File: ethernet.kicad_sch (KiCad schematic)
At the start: 116 parts, among them IC2 ACPL-217-500E, J2 5-2337992-8, U13 TPS2372-3RGWR, U16 TS3L500, U6 KSZ9031RNXCA, Y1 ABM8G-25.000MHZ-18-D2Y-T

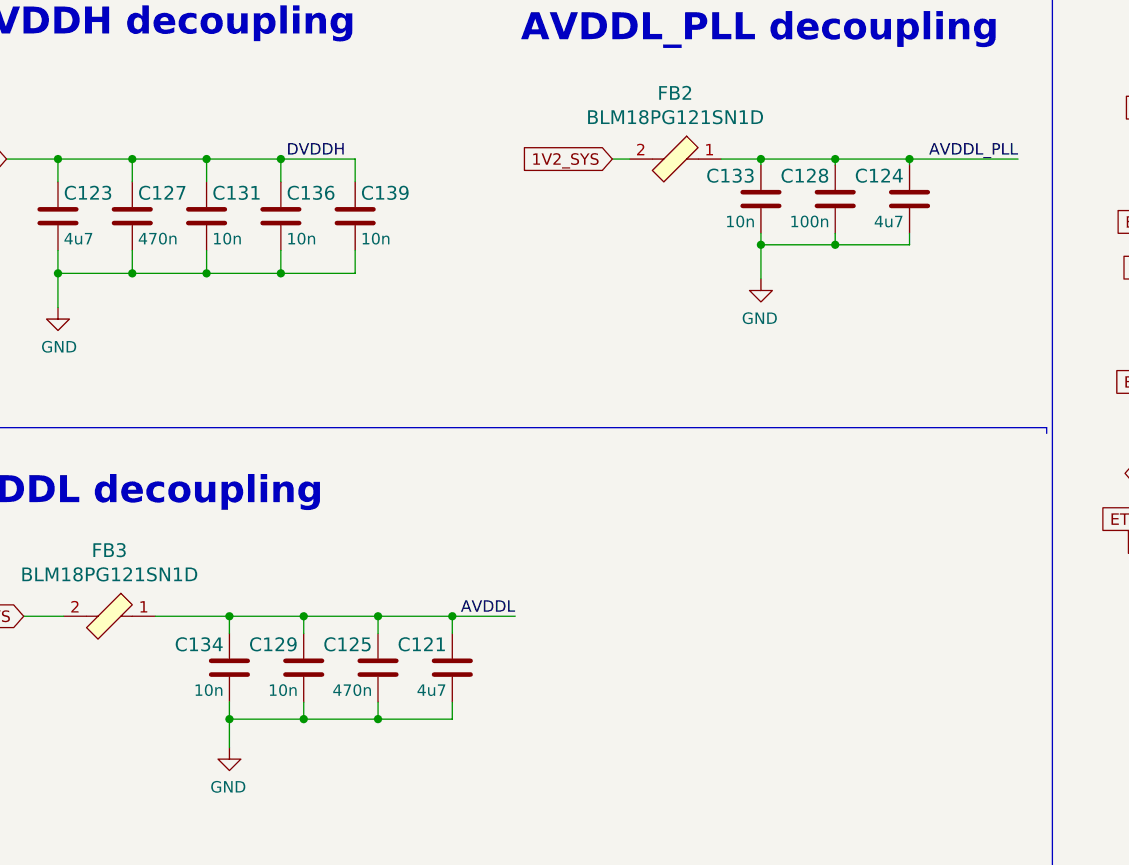
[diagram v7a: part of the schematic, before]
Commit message: Readability improvements
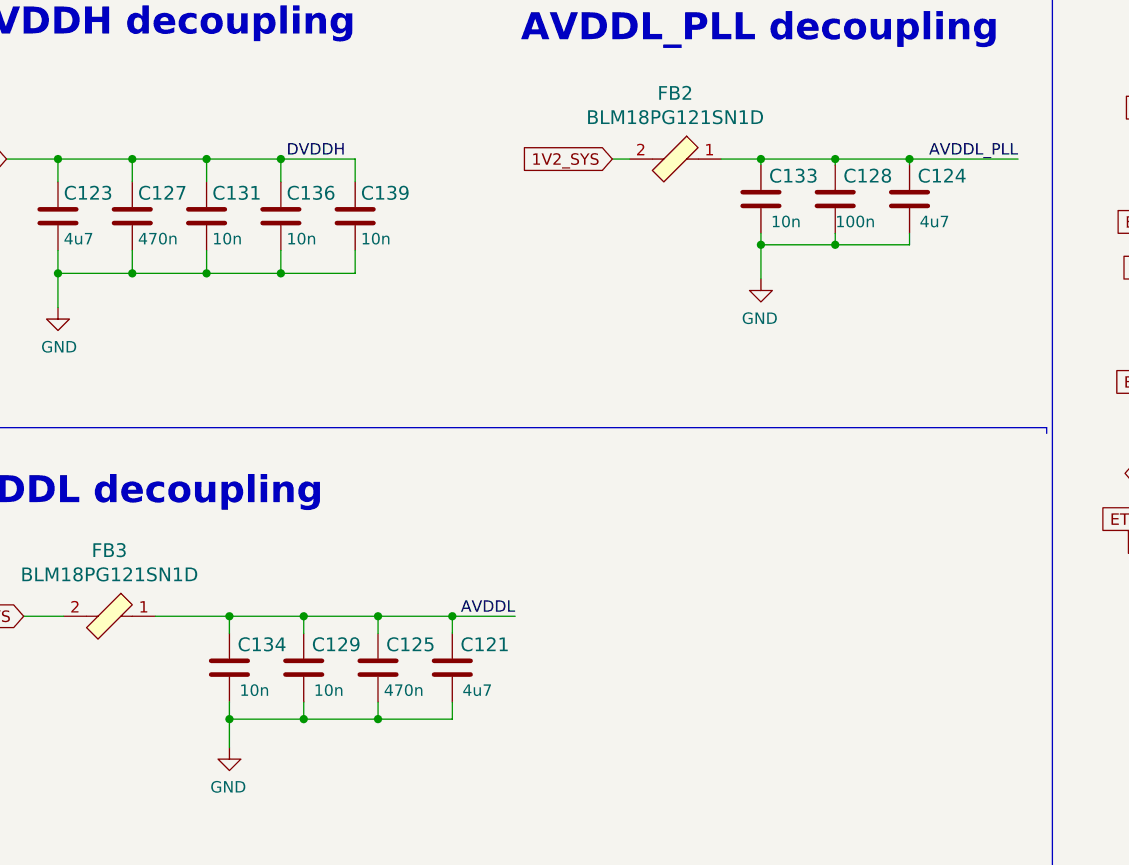
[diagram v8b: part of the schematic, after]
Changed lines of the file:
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@@
   (symbol (lib_id "data-center-dram-tester:C_4u7_0402") (at 73.66 145.415 0) (mirror y) (unit 1)
     (in_bom yes) (on_board yes)
-    (property "Reference" "C121" (id 0) (at 73.025 142.875 0)
+    (property "Reference" "C121" (id 0) (at 80.01 142.875 0)
       (effects (font (size 1.524 1.524)) (justify left))
     )
@@
       (effects (font (size 1.524 1.524)) (justify left) hide)
     )
-    (property "Val" "4u7" (id 6) (at 73.025 147.955 0)
+    (property "Val" "4u7" (id 6) (at 78.105 147.955 0)
       (effects (font (size 1.27 1.27)) (justify left))
     )
@@
   (symbol (lib_id "data-center-dram-tester:C_470n_0402") (at 65.405 145.415 0) (mirror y) (unit 1)
     (in_bom yes) (on_board yes)
-    (property "Reference" "C125" (id 0) (at 64.77 142.875 0)
+    (property "Reference" "C125" (id 0) (at 71.755 142.875 0)
       (effects (font (size 1.524 1.524)) (justify left))
     )
@@
       (effects (font (size 1.524 1.524)) (justify left) hide)
     )
-    (property "Val" "470n" (id 6) (at 64.77 147.955 0)
+    (property "Val" "470n" (id 6) (at 70.485 147.955 0)
       (effects (font (size 1.27 1.27)) (justify left))
     )
@@
   (symbol (lib_id "data-center-dram-tester:C_10n_0402") (at 57.15 145.415 0) (mirror y) (unit 1)
     (in_bom yes) (on_board yes)
-    (property "Reference" "C129" (id 0) (at 56.515 142.875 0)
+    (property "Reference" "C129" (id 0) (at 63.5 142.875 0)
       (effects (font (size 1.524 1.524)) (justify left))
     )
@@
       (effects (font (size 1.524 1.524)) (justify left) hide)
     )
-    (property "Val" "10n" (id 6) (at 56.515 147.955 0)
+    (property "Val" "10n" (id 6) (at 61.595 147.955 0)
       (effects (font (size 1.27 1.27)) (justify left))
     )
@@
   (symbol (lib_id "data-center-dram-tester:C_10n_0402") (at 48.895 145.415 0) (mirror y) (unit 1)
     (in_bom yes) (on_board yes)
-    (property "Reference" "C134" (id 0) (at 48.26 142.875 0)
+    (property "Reference" "C134" (id 0) (at 55.245 142.875 0)
       (effects (font (size 1.524 1.524)) (justify left))
     )
@@
       (effects (font (size 1.524 1.524)) (justify left) hide)
     )
-    (property "Val" "10n" (id 6) (at 48.26 147.955 0)
+    (property "Val" "10n" (id 6) (at 53.34 147.955 0)
       (effects (font (size 1.27 1.27)) (justify left))
     )
@@
   (symbol (lib_id "data-center-dram-tester:C_100n_0402_16V") (at 116.205 93.345 0) (mirror y) (unit 1)
     (in_bom yes) (on_board yes)
-    (property "Reference" "C128" (id 0) (at 115.57 90.805 0)
+    (property "Reference" "C128" (id 0) (at 122.555 90.805 0)
       (effects (font (size 1.524 1.524)) (justify left))
     )
@@
       (effects (font (size 1.524 1.524)) (justify left) hide)
     )
-    (property "Val" "100n" (id 6) (at 115.57 95.885 0)
+    (property "Val" "100n" (id 6) (at 120.65 95.885 0)
       (effects (font (size 1.27 1.27)) (justify left))
     )
@@
   (symbol (lib_id "data-center-dram-tester:C_4u7_0402") (at 124.46 93.345 0) (mirror y) (unit 1)
     (in_bom yes) (on_board yes)
-    (property "Reference" "C124" (id 0) (at 123.825 90.805 0)
+    (property "Reference" "C124" (id 0) (at 130.81 90.805 0)
       (effects (font (size 1.524 1.524)) (justify left))
     )
@@
       (effects (font (size 1.524 1.524)) (justify left) hide)
     )
-    (property "Val" "4u7" (id 6) (at 123.825 95.885 0)
+    (property "Val" "4u7" (id 6) (at 128.905 95.885 0)
       (effects (font (size 1.27 1.27)) (justify left))
     )
@@
   (symbol (lib_id "data-center-dram-tester:C_10n_0402") (at 107.95 93.345 0) (mirror y) (unit 1)
     (in_bom yes) (on_board yes)
-    (property "Reference" "C133" (id 0) (at 107.315 90.805 0)
+    (property "Reference" "C133" (id 0) (at 114.3 90.805 0)
       (effects (font (size 1.524 1.524)) (justify left))
     )
@@
       (effects (font (size 1.524 1.524)) (justify left) hide)
     )
-    (property "Val" "10n" (id 6) (at 107.315 95.885 0)
-      (effects (font (size 1.27 1.27)) (justify left))
-    )
+    (property "Val" "10n" (id 6) (at 112.395 95.885 0)
+      (effects (font (size 1.27 1.27)) (justify left))
+    )
